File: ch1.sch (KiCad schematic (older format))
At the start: 29 parts

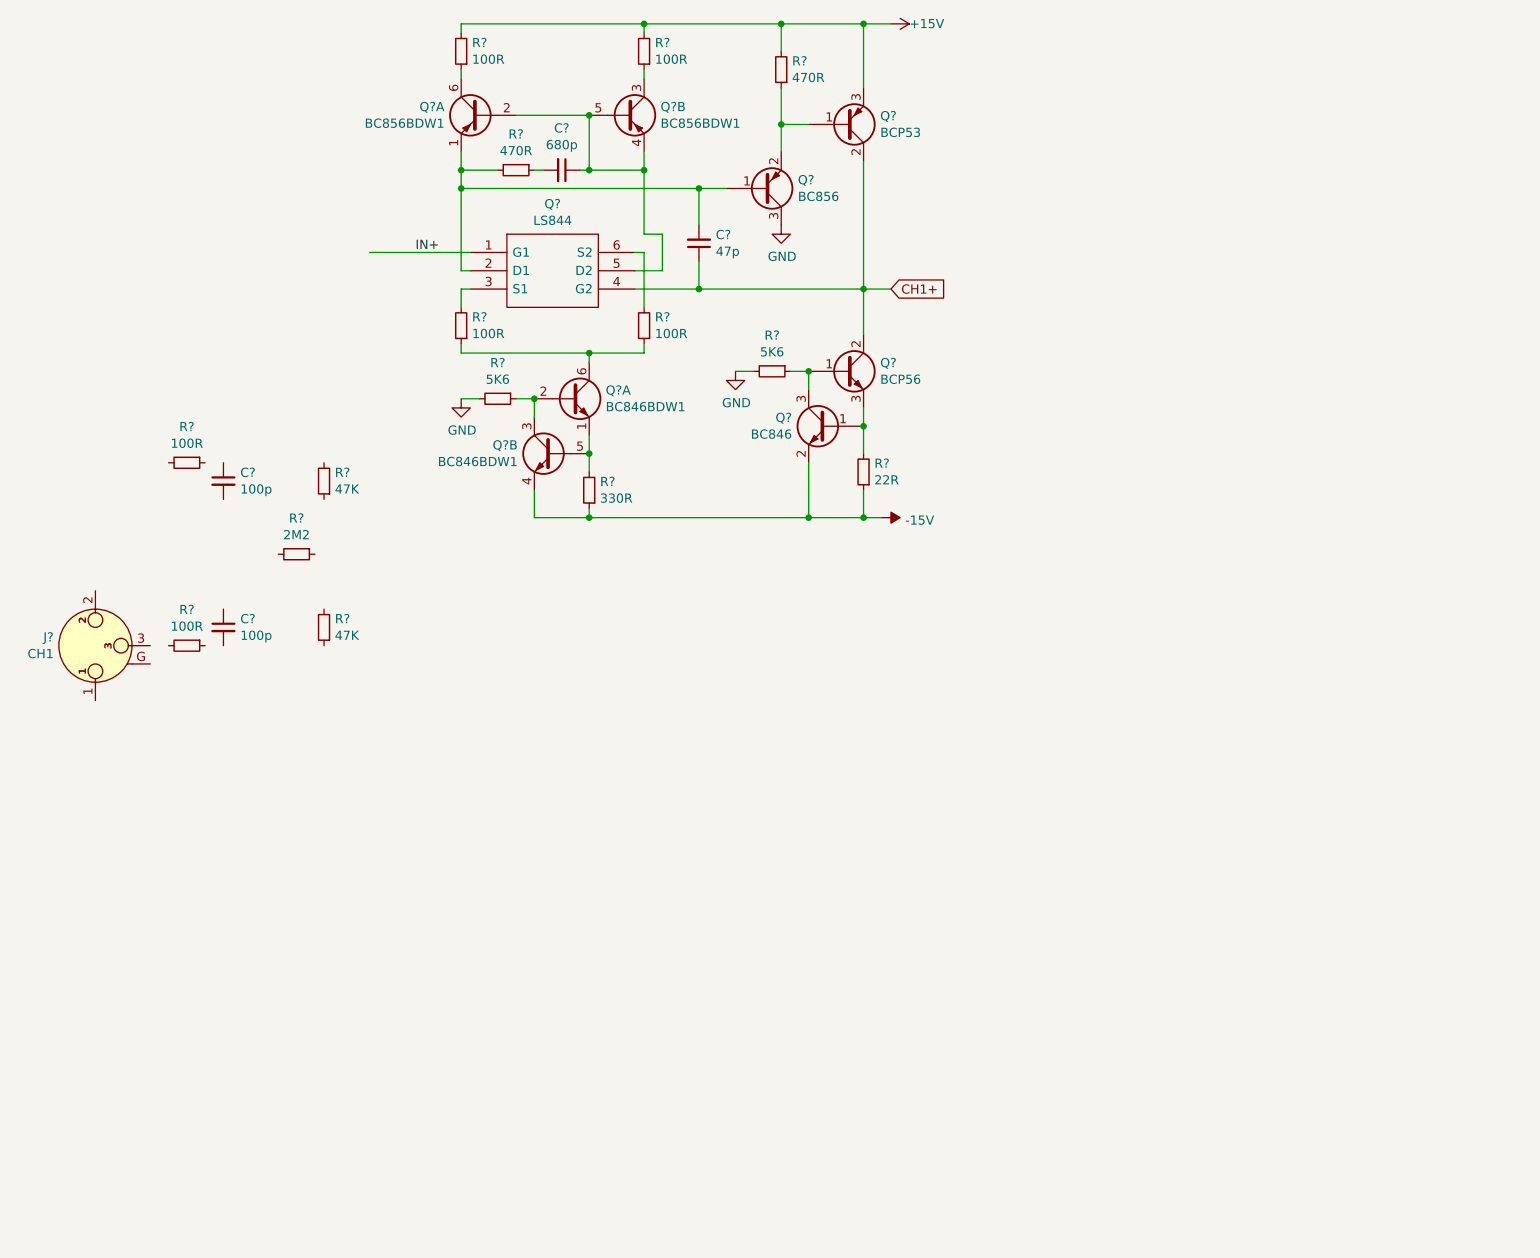
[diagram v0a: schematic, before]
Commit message: added pages and buffer schematics
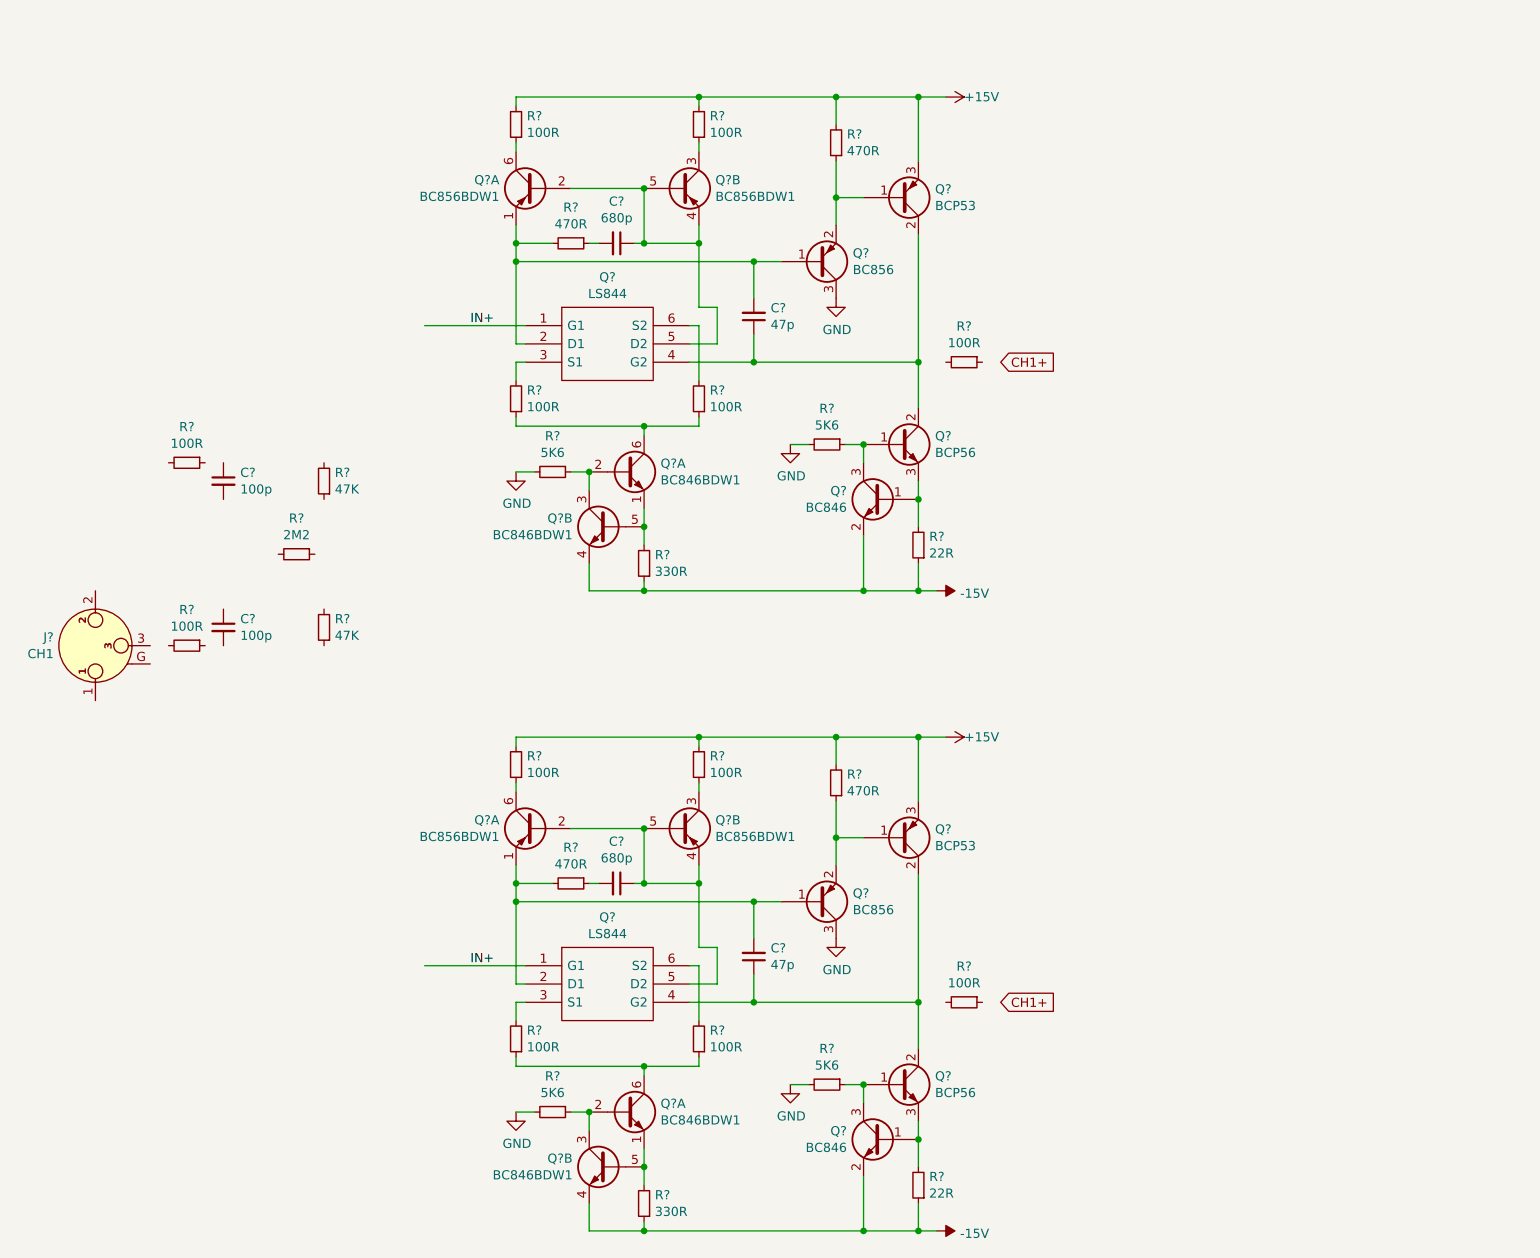
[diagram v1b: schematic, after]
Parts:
- added C?: 680p, symbol Device:C_Small
- added C?: 47p, symbol Device:C_Small
- added Q?: LS844, SOT95P280X145-6N, symbol LS844-SOT-23-6L-CT:LS844-SOT-23-6L-CT
- added Q?: BC856, Package_TO_SOT_SMD:SOT-23, symbol Transistor_BJT:BC856
- added Q?: BC846, Package_TO_SOT_SMD:SOT-23, symbol Transistor_BJT:BC846
- added Q? (x2): BC846BDW1, Package_TO_SOT_SMD:SOT-363_SC-70-6, symbol Transistor_BJT:BC846BDW1
- added Q? (x2): BC856BDW1, Package_TO_SOT_SMD:SOT-363_SC-70-6, symbol Transistor_BJT:BC856BDW1
- added Q?: BCP53, Package_TO_SOT_SMD:SOT-223-3_TabPin2, symbol Transistor_BJT:BCP53
- added Q?: BCP56, Package_TO_SOT_SMD:SOT-223-3_TabPin2, symbol Transistor_BJT:BCP56
- added R? (x6): 100R, symbol Device:R_Small
- added R? (x2): 470R, symbol Device:R_Small
- added R? (x2): 5K6, symbol Device:R_Small
- added R?: 330R, symbol Device:R_Small
- added R?: 22R, symbol Device:R_Small
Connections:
- net +15V: now also Q?.3 (E), R?.2, R?.2, R?.2
- net -15V: now also Q?.2 (E), Q?.4 (E2), R?.1, R?.1
- net CH1+: no longer C?.1, Q?.2 (C), Q?.2 (C), Q?.4 (C), Q?.4 (C), Q?.4 (G2)
- net GND: now also Q?.3 (C), R?.2, R?.2
- net IN+: now also Q?.1 (G1)
- new net: C?.1, Q?.2 (C), Q?.2 (C), Q?.4 (C), Q?.4 (C), Q?.4 (G2) (x2)
- new net: C?.2, Q?.1 (B), Q?.1 (E1), Q?.2 (D1), R?.2
- new net: Q?.3 (S1), R?.2
- new net: C?.1, Q?.2 (B1), Q?.4 (E2), Q?.5 (B2), Q?.5 (D2)
- new net: Q?.6 (S2), R?.2
- new net: C?.2, R?.1
- new net: Q?.6 (C1), R?.1
- new net: Q?.3 (C2), R?.1
- new net: Q?.6 (C1), R?.1, R?.1
- new net: Q?.2 (B1), Q?.3 (C2), R?.1
- new net: Q?.1 (E1), Q?.5 (B2), R?.2
- new net: Q?.1 (B), Q?.2 (E), R?.1
- new net: Q?.1 (B), Q?.3 (E), R?.2
- new net: Q?.1 (B), Q?.3 (C), R?.1
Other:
- moved on the sheet: C?, Q?, Q?A, Q?B, R?

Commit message: ch1 and ch2 are complete
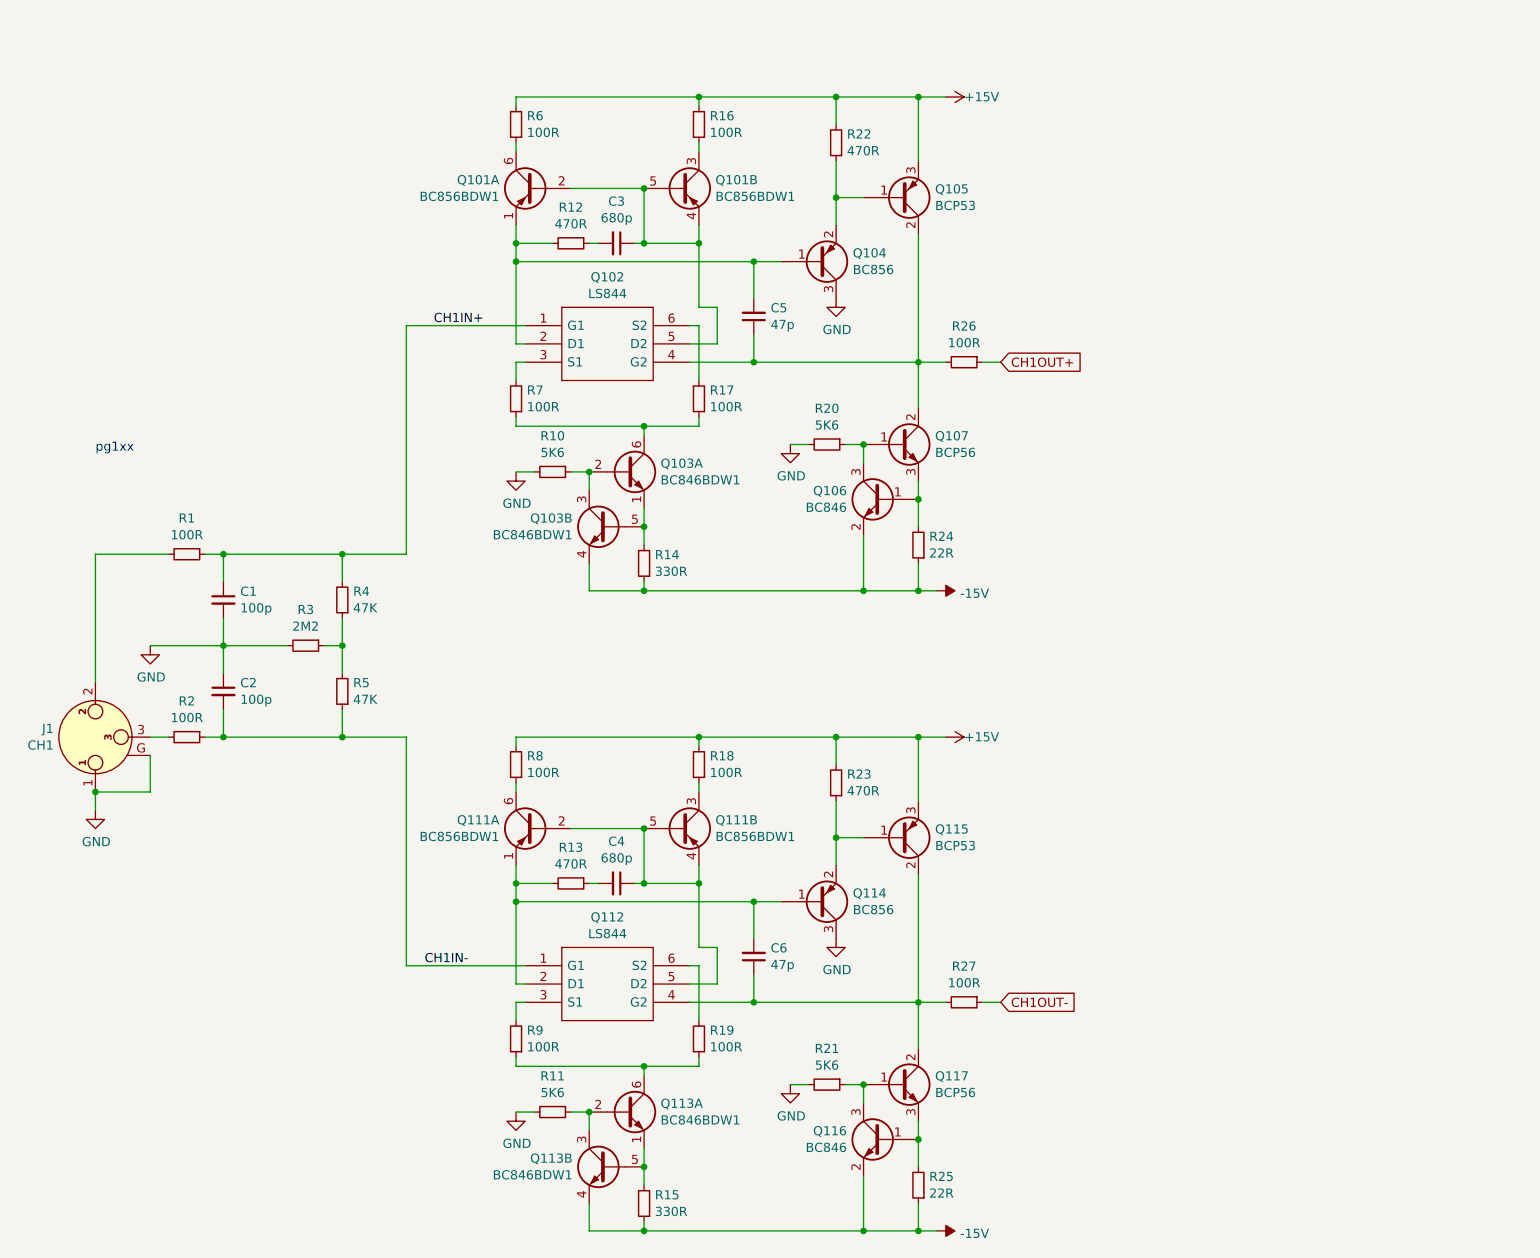
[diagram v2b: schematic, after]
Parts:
- gave numbers to parts that had none: 48
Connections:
- net GND: now also C1.2, C2.1, J1.1, J1.G, R3.2
- net at J1.2: now also R1.2
- net at J1.3: now also R2.2
- net CH1IN+: now reaches R1.1
- net CH1IN+: now also C1.1, Q102.1 (G1), R4.2
- net CH1IN-: now reaches R2.1
- net CH1IN-: now also C2.2, Q112.1 (G1), R5.1
- net at R3.1: now also R4.1, R5.2
- net at C5.1, Q102.4 (G2), Q105.2 (C)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: now also R26.2
- net CH1OUT+: now reaches R26.1
- net at C6.1, Q112.4 (G2), Q115.2 (C)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: now also R27.2
- net CH1OUT-: now reaches R27.1
- removed net IN+: Q102.1 (G1), Q112.1 (G1)
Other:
- note added: "pg1xx"
- moved on the sheet: C1, C2, J1, R1, R2, R3, R4, R5

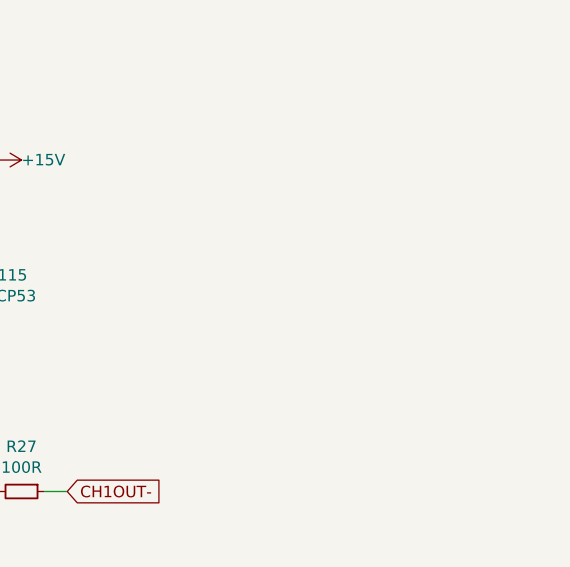
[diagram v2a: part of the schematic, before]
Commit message: assigned footprints
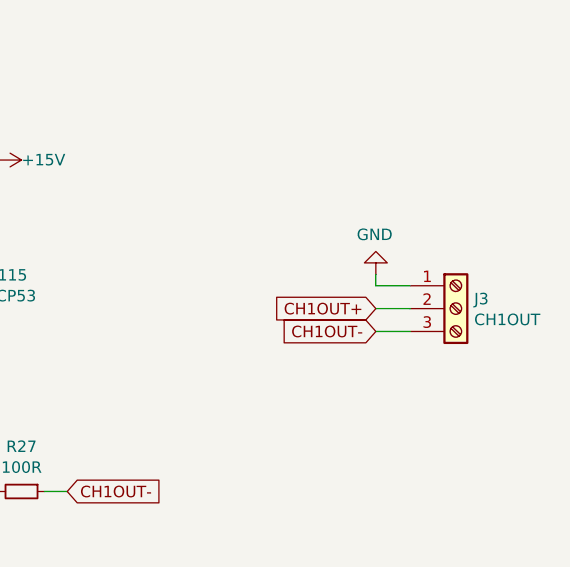
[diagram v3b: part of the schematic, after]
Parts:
- added J3: CH1OUT, TerminalBlock_Phoenix:TerminalBlock_Phoenix_PT-1,5-3-3.5-H_1x03_P3.50mm_Horizontal, symbol Connector:Screw_Terminal_01x03
- C1, C2, C3, C4, C5, C6: footprint (none) -> Capacitor_SMD:C_0805_2012Metric_Pad1.15x1.40mm_HandSolder
- J1: footprint (none) -> Connector_Audio:Jack_XLR_Neutrik_NC3FAAH2_Horizontal
- Q102, Q112: footprint SOT95P280X145-6N -> Package_TO_SOT_SMD:SOT-23-6
- R1, R10, R11, R12, R13, R14, R15, R16, R17, R18, R19, R2, R20, R21, R22, R23, R24, R25, R26, R27, R3, R4, R5, R6, R7, R8, R9: footprint (none) -> Resistor_SMD:R_0805_2012Metric_Pad1.15x1.40mm_HandSolder
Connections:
- net CH1OUT+: now also J3.2 (Pin_2)
- net CH1OUT-: now also J3.3 (Pin_3)
- net GND: now also J3.1 (Pin_1)
